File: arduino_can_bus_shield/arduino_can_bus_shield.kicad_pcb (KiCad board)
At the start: 2 copper layers, 68.6 x 53.3 mm, 8 parts, among them P1 Power, P2 Analog, P3 Digital, P4 Digital, P5 CONN_01X01, P6 CONN_01X01, P7 CONN_01X01, P8 CONN_01X01

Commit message: ohh
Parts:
- removed P5, P6, P7, P8: CONN_01X01, Socket_Arduino_Uno:Arduino_1pin
- added C1: 22pF, Capacitor_SMD:C_0805_2012Metric_Pad1.18x1.45mm_HandSolder, F.Cu at (124.4, 92.1)
- added C2: 22pF, Capacitor_SMD:C_0805_2012Metric_Pad1.18x1.45mm_HandSolder, F.Cu at (124.7, 101.3)
- added C3 100nF: 100nF, Capacitor_SMD:C_0805_2012Metric_Pad1.18x1.45mm_HandSolder, F.Cu at (146.8, 89.7)
- added C4: 100nF, Capacitor_SMD:C_0805_2012Metric_Pad1.18x1.45mm_HandSolder, F.Cu at (141.6, 102.9)
- added D1: power, LED_SMD:LED_0805_2012Metric_Pad1.15x1.40mm_HandSolder, F.Cu at (120.1, 81.3)
- added G***: LOGO, PolyuRobotics:Club_logo, F.Cu at (135.4, 80.9)
- added J1: molex_3.0, Connector_Molex:Molex_Micro-Fit_3.0_43045-0421_2x02-1MP_P3.00mm_Horizontal, F.Cu at (140.4, 117.6)
- added J2: molex_3.0, Connector_Molex:Molex_Micro-Fit_3.0_43045-0421_2x02-1MP_P3.00mm_Horizontal, F.Cu at (127.7, 117.5)
- added J5: jumper, Connector_PinHeader_2.54mm:PinHeader_1x02_P2.54mm_Vertical, F.Cu at (133.3, 108.5)
- added J6: UART2, Connector_PinSocket_2.54mm:PinSocket_1x04_P2.54mm_Vertical, F.Cu at (150.9, 123.3)
- added R1 17K: 17K, Resistor_SMD:R_0805_2012Metric_Pad1.20x1.40mm_HandSolder, F.Cu at (147.0, 97.0)
- added R2 10K: 10K, Resistor_SMD:R_0805_2012Metric_Pad1.20x1.40mm_HandSolder, F.Cu at (146.8, 92.1)
- added R3: 120, Resistor_SMD:R_0805_2012Metric_Pad1.20x1.40mm_HandSolder, F.Cu at (130.1, 106.7)
- added R4 10K: 10K, Resistor_SMD:R_0805_2012Metric_Pad1.20x1.40mm_HandSolder, F.Cu at (120.1, 83.7)
- added R5 10K: 10K, Resistor_SMD:R_0805_2012Metric_Pad1.20x1.40mm_HandSolder, F.Cu at (146.8, 87.1)
- added SW1: User, Button_Switch_SMD:SW_Push_1P1T_NO_6x6mm_H9.5mm, F.Cu at (153.9, 82.0)
- added U1: MCP2515-xST, Package_SO:TSSOP-20_4.4x6.5mm_P0.65mm, F.Cu at (138.7, 94.4)
- added U2: MCP2551-I-SN, Package_SO:SOIC-8_3.9x4.9mm_P1.27mm, F.Cu at (148.2, 102.7)
- added Y1: 16MHz, Crystal:Crystal_HC49-U_Vertical, F.Cu at (130.5, 94.1)
- moved P2 49.7 mm to (113.8, 110.9), turned to -90 degrees
- moved P1 43.8 mm to (113.8, 88.0), turned to -90 degrees
- moved P3 32.4 mm to (162.1, 78.9), turned to -90 degrees
- moved P4 30.7 mm to (162.1, 105.8), turned to -90 degrees
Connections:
- net /10(**/SS) renamed /10(**/SS)
- P1 pad 1: Net-(P1-Pad1) -> unconnected-(P1-Pad1)
- P3 pad 1: /A5(SCL) -> unconnected-(P3-Pad1)
- P3 pad 2: /A4(SDA) -> unconnected-(P3-Pad2)
- P3 pad 7: /11(**/MOSI) -> /11(**/MOSI)
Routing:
- net +5V: track 0.00 -> 169.2 mm, vias 0 -> 2
- net /CAN-: track 0.00 -> 60.6 mm, vias 0 -> 1
- net /CAN+: track 0.00 -> 56.3 mm
- net /5(**): track 0.00 -> 37.1 mm, vias 0 -> 2
- net /7: track 0.00 -> 34.1 mm, vias 0 -> 1
- net /13(SCK): track 0.00 -> 25.6 mm
- net /11(**/MOSI): track 0.00 -> 22.3 mm, vias 0 -> 1
- net /CAN_Rx: track 0.00 -> 22.1 mm
- net /12(MISO): track 0.00 -> 21.4 mm, vias 0 -> 1
- net /CAN_Tx: track 0.00 -> 17.3 mm
- net /1(Tx): track 0.00 -> 12.3 mm
- net /0(Rx): track 0.00 -> 12.3 mm
- net Net-(C2-Pad1): track 0.00 -> 12.0 mm
- net Net-(C1-Pad1): track 0.00 -> 12.0 mm
- net Net-(R1-Pad1): track 0.00 -> 7.00 mm
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- added copper zone on B.Cu, net GND
- added copper zone on F.Cu, net GND
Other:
- board size 68.6 x 53.3 mm -> 53.3 x 51.8 mm
- board text added: "100pF"
- board text added: "120"
- board text added: "16MHz"
- board text added: "22pF"
- board text added: "5v"
- board text added: "Arduino CAN-BUS shield v1.0 2022-1-30 Samson Chau"
- board text added: "GND"
- board text added: "MCP2515"
- board text added: "MCP2551"
- board text added: "Rx"
- board text added: "Tx"
- board text added: "UART"
- board text added: "power"

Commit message: Raymond
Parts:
- added G***: LOGO, PolyuRobotics:Raymond, B.Cu at (149.6, 100.6)
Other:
- board text added: "在埋土裡尋求乞食是否搞錯了什麼"

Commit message: mod plug
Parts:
- C3: renamed from C3 100nF
- J1, J2: footprint Connector_Molex:Molex_Micro-Fit_3.0_43045-0421_2x02-1MP_P3.00mm_Horizontal -> Connector_Molex:Molex_Micro-Fit_3.0_43045-0400_2x02_P3.00mm_Horizontal
- R1: renamed from R1 17K
- R2: renamed from R2 10K
- R4: renamed from R4 10K
- R5: renamed from R5 10K

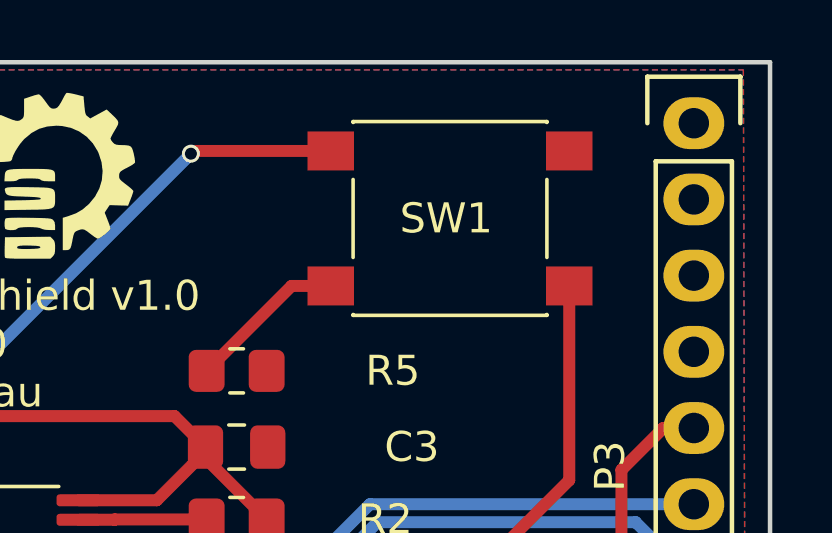
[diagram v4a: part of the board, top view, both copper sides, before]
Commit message: fix design in arduinoshield
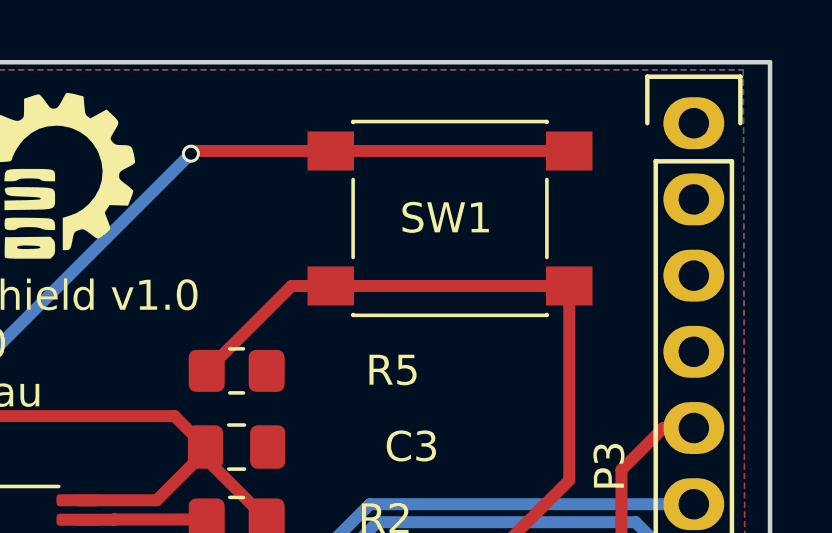
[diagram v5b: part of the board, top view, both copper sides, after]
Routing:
- net /5(**): track 37.1 -> 45.1 mm
- net +5V: track 169.2 -> 177.1 mm
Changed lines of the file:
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@@
   (segment (start 117.602 96.012) (end 115.443 98.171) (width 0.4) (layer "F.Cu") (net 3))
   (segment (start 145.7745 90.0375) (end 147.812 92.075) (width 0.4) (layer "F.Cu") (net 3))
+  (segment (start 157.899 79.792) (end 149.949 79.792) (width 0.4) (layer "F.Cu") (net 3))
   (segment (start 117.602 90.17) (end 117.856 89.916) (width 0.4) (layer "F.Cu") (net 3))
   (segment (start 141.605 103.9075) (end 139.0865 103.9075) (width 0.4) (layer "F.Cu") (net 3))
@@
   (segment (start 157.899 90.767) (end 154.813 93.853) (width 0.4) (layer "F.Cu") (net 17))
   (segment (start 160.401 110.871) (end 162.052 110.871) (width 0.4) (layer "F.Cu") (net 17))
+  (segment (start 149.949 84.292) (end 157.899 84.292) (width 0.4) (layer "F.Cu") (net 17))
   (via (at 158.496 99.822) (size 0.6) (drill 0.4) (layers "F.Cu" "B.Cu") (net 17))
   (via (at 154.813 93.853) (size 0.6) (drill 0.4) (layers "F.Cu" "B.Cu") (net 17))

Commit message: POS_CARD
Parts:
- C3 100nF: renamed from C3
- R2 10K: renamed from R2
- R5 10K: renamed from R5
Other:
- board text added: "10K"
- board text added: "GPIO 5"
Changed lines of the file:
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@@
     (property "Sheetname" "")
     (attr smd)
-    (fp_text reference "R4" (at -4.953 0) (layer "F.SilkS")
+    (fp_text reference "R4" (at -3.175 -0.127) (layer "F.SilkS")
       (effects (font (size 1 1) (thickness 0.15)))
     )
@@
     (property "Sheetname" "")
     (attr smd)
-    (fp_text reference "R2" (at -4.953 0) (layer "F.SilkS")
+    (fp_text reference "R2 10K" (at -5.334 0) (layer "F.SilkS")
       (effects (font (size 1 1) (thickness 0.15)))
     )
@@
     (property "Sheetname" "")
     (attr smd)
-    (fp_text reference "C3" (at 5.842 0) (layer "F.SilkS")
+    (fp_text reference "C3 100nF" (at 6.096 0) (layer "F.SilkS")
       (effects (font (size 1 1) (thickness 0.15)))
     )
@@
     (property "Sheetname" "")
     (attr smd)
-    (fp_text reference "R5" (at 5.207 0) (layer "F.SilkS")
+    (fp_text reference "R5 10K" (at 5.207 0) (layer "F.SilkS")
       (effects (font (size 1 1) (thickness 0.15)))
     )
@@
     (effects (font (size 1 1) (thickness 0.15)))
   )
+  (gr_text "GPIO 5" (at 153.924 78.105) (layer "F.SilkS")
+    (effects (font (size 1 1) (thickness 0.15)))
+  )
   (gr_text "120\n" (at 128.397 106.68 90) (layer "F.SilkS")
     (effects (font (size 1 1) (thickness 0.15)))
@@
     (effects (font (size 1 1) (thickness 0.15)))
   )
+  (gr_text "10K\n" (at 116.84 85.09) (layer "F.SilkS")
+    (effects (font (size 1 1) (thickness 0.15)))
+  )
